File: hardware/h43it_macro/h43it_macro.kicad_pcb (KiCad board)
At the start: 2 copper layers, 90 x 90 mm, 43 parts, among them J1 Conn_01x04_Pin, SW2 SW_Push, U1 ATtiny816-M

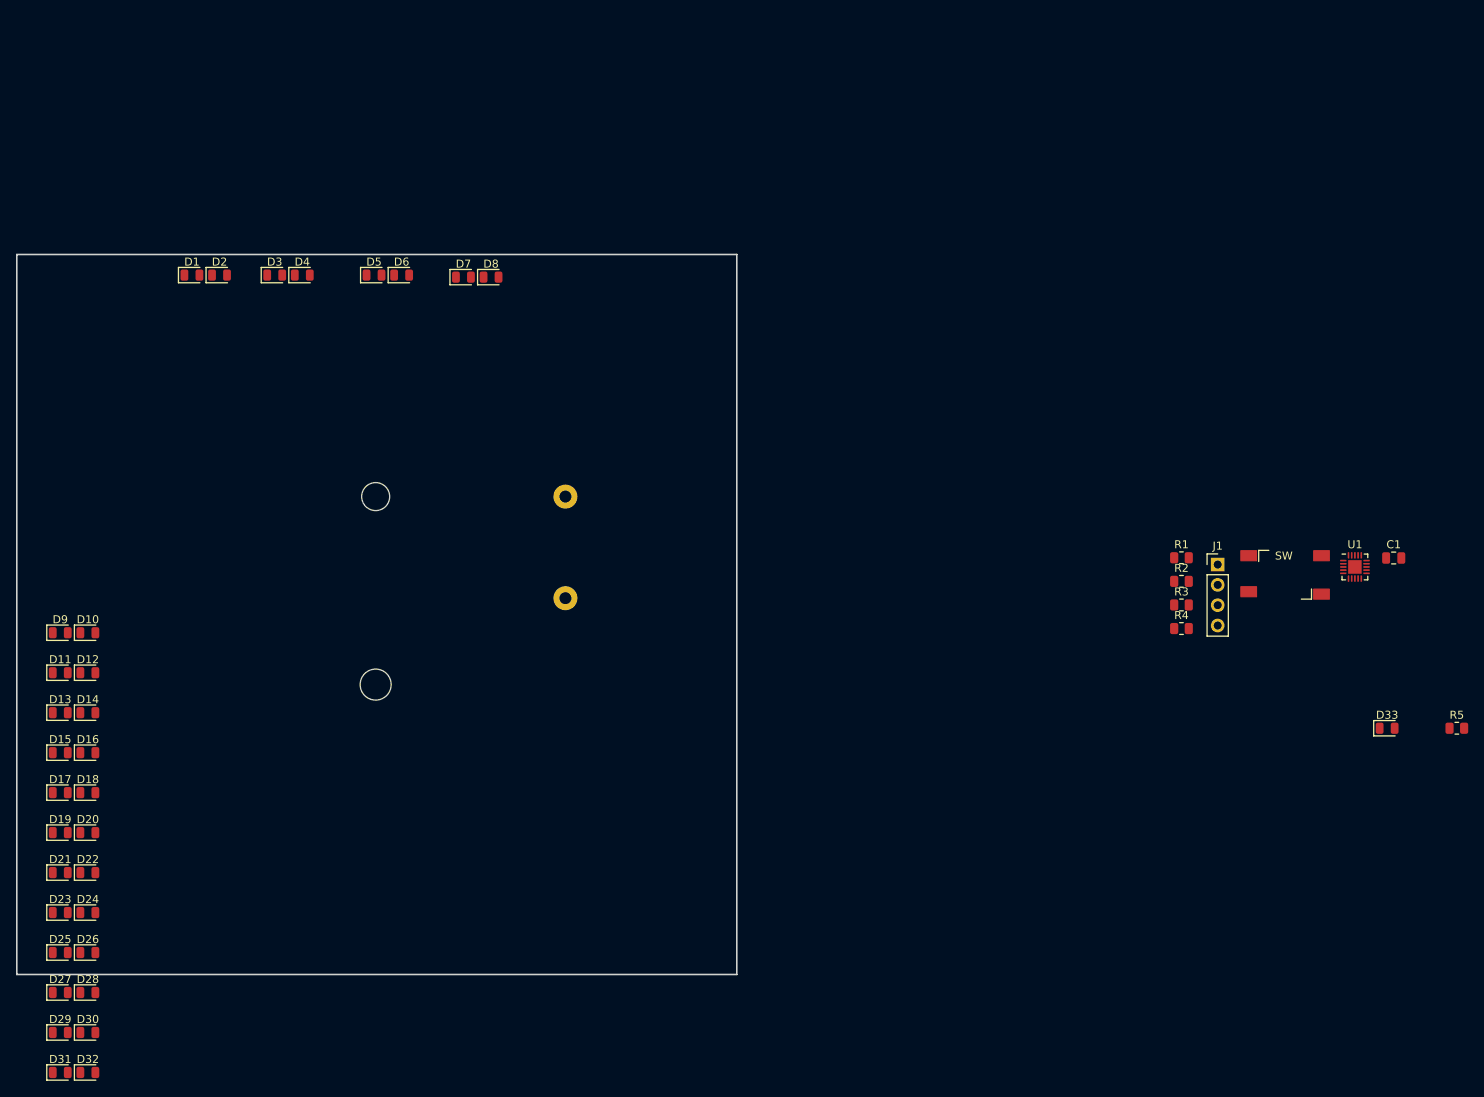
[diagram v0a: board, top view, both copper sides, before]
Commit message: add twin attiny 816
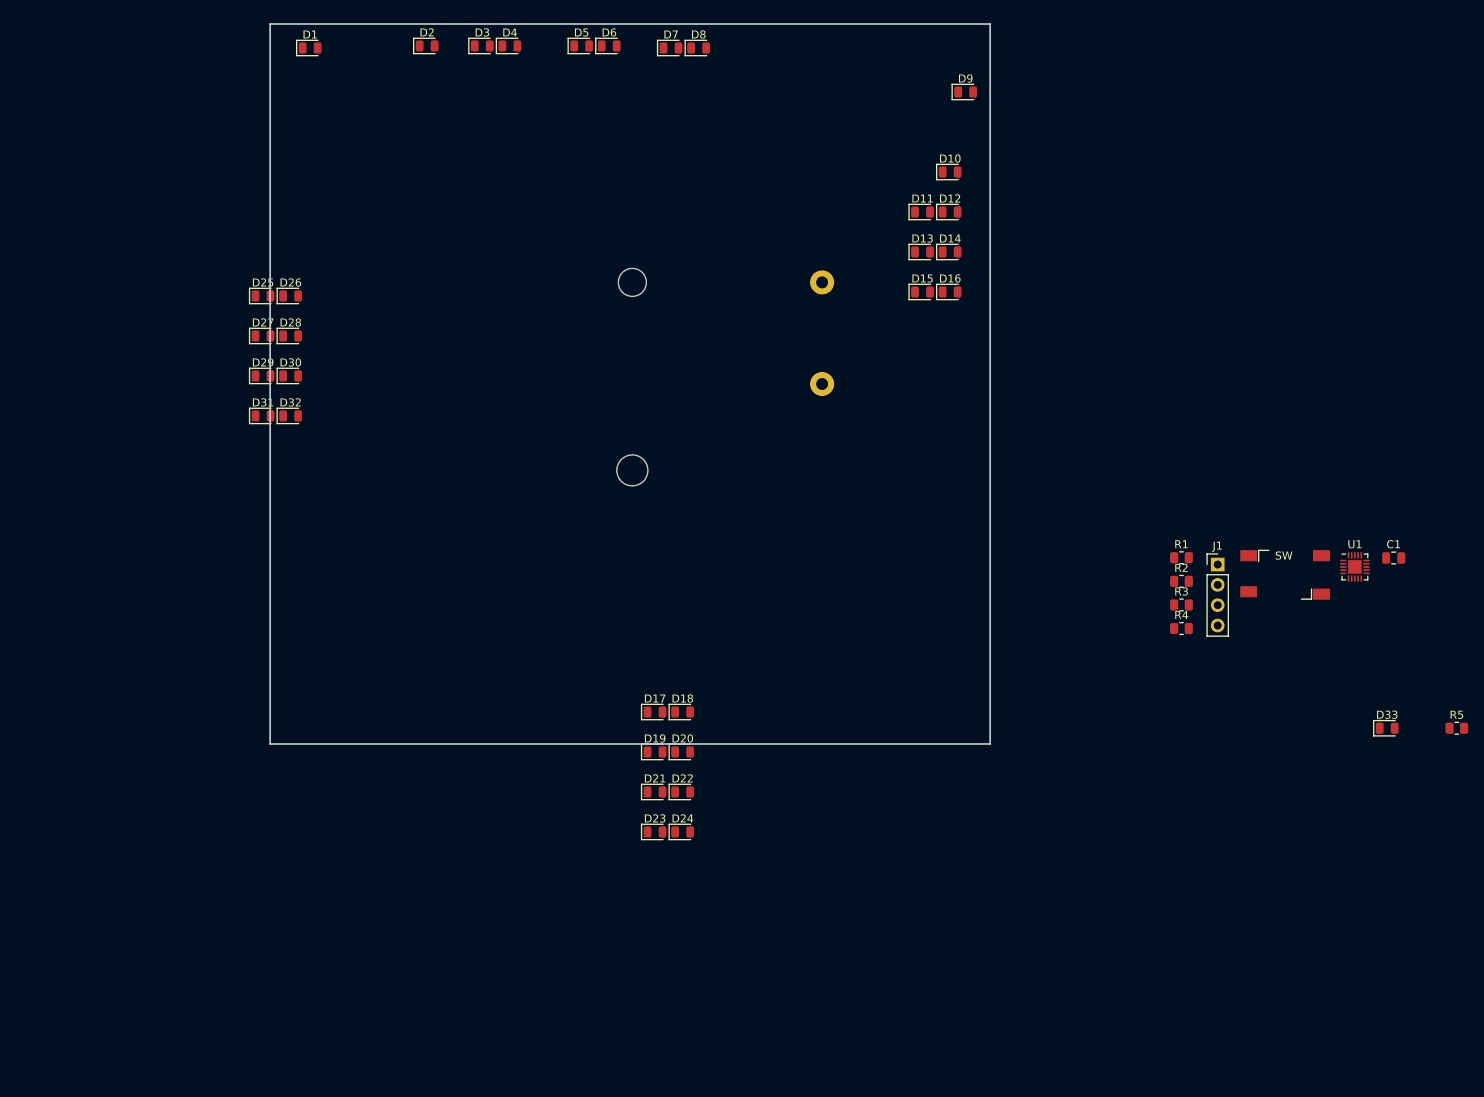
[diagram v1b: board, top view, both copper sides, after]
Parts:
- moved D9 131.8 mm to (156.9, 33.5)
- moved D10 122.2 mm to (155.0, 43.5)
- moved D11 122.2 mm to (151.6, 48.5)
- moved D12 122.2 mm to (155.0, 48.5)
- moved D13 122.2 mm to (151.6, 53.5)
- moved D14 122.2 mm to (155.0, 53.5)
- moved D15 122.2 mm to (151.6, 58.5)
- moved D16 122.2 mm to (155.0, 58.5)
- moved D25 85.9 mm to (69.1, 59.0)
- moved D26 85.9 mm to (72.6, 59.0)
- moved D29 85.9 mm to (69.1, 69.0)
- moved D30 85.9 mm to (72.6, 69.0)
- moved D27 85.9 mm to (69.1, 64.0)
- moved D28 85.9 mm to (72.6, 64.0)
- moved D31 85.9 mm to (69.1, 74.0)
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
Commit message: pcb for macro
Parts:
- removed U1: ATtiny816-M, Package_DFN_QFN:VQFN-20-1EP_3x3mm_P0.4mm_EP1.7x1.7mm
- added C2: 100pF, Capacitor_SMD:C_0805_2012Metric, F.Cu at (130.9, 100.0)
- added C3: 1uF, Capacitor_SMD:C_0805_2012Metric, F.Cu at (128.0, 100.0)
- added C4: 100pF, Capacitor_SMD:C_0805_2012Metric, F.Cu at (129.9, 95.0)
- added U2: ~, MyLib:TSOT32-6, F.Cu at (129.8, 89.6)
- added U4: ATtiny816-S, Package_SO:SOIC-20W_7.5x12.8mm_P1.27mm, F.Cu at (115.0, 94.1)
- added U6: ~, MyLib:TouchButton-15x10mm, F.Cu at (115.0, 70.0)
- BT1: footprint MyLib:Battery_holder_AAA_534-2479 -> MyLib:Battery_holder__Keystone_Electronic_AA_2462
- R5: value 100Ω -> 27Ω
- moved R5 119.0 mm to (100.9, 94.0), turned to 90 degrees
- moved D33 115.2 mm to (96.0, 94.0), turned to -90 degrees
- moved R4 105.2 mm to (84.4, 66.7)
- moved SW2 90.2 mm to (114.7, 56.3)
- moved R1 86.0 mm to (116.0, 38.9), turned to -90 degrees
- moved C1 84.6 mm to (126.0, 96.0)
- moved R3 68.7 mm to (116.0, 108.1), turned to 90 degrees
- moved J1 46.3 mm to (142.2, 90.3)
- moved D25 45.4 mm to (74.9, 104.0), turned to 180 degrees
- moved R2 45.0 mm to (148.6, 66.7)
- moved D17 30.2 mm to (148.4, 110.9), turned to -90 degrees
- moved BT1 25.0 mm to (115.0, 70.0)
- moved D8 23.9 mm to (147.4, 29.1)
- moved D10 23.8 mm to (154.4, 67.3)
- moved D11 23.8 mm to (150.9, 72.3)
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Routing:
- net Net-(U2-CX): track 0.00 -> 27.4 mm
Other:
- outline, holes or cut-outs redrawn
- board text added: "TOUCH ME!"

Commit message: pcb for macro
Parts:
- moved SW2 7.91 mm to (114.7, 48.4)
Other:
- board text added: "TOUCH ME IF YOU CAN"
- board text removed: "TOUCH ME!"
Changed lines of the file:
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@@
   )
   (footprint "MyLib:FSM2JSMAATR" (layer "F.Cu")
-    (at 114.746 56.32)
+    (at 114.746 48.41)
     (property "Sheetfile" "h43it_macro.kicad_sch")
     (property "Sheetname" "")
@@
   (gr_line locked (start 80 115) (end 150 115)
     (stroke (width 0.1) (type default)) (layer "Edge.Cuts"))
-  (gr_text "TOUCH ME!" (at 104.078 64.158) (layer "F.SilkS")
-    (effects (font (size 3 3) (thickness 0.3) bold) (justify left bottom))
+  (gr_text "TOUCH ME \nIF YOU CAN" (at 116.016 63.396) (layer "F.SilkS")
+    (effects (font (size 3 3) (thickness 0.3) bold) (justify bottom))
   )
   (segment (start 133 87) (end 131.326 88.674) (width 0.25) (layer "F.Cu") (net 28))

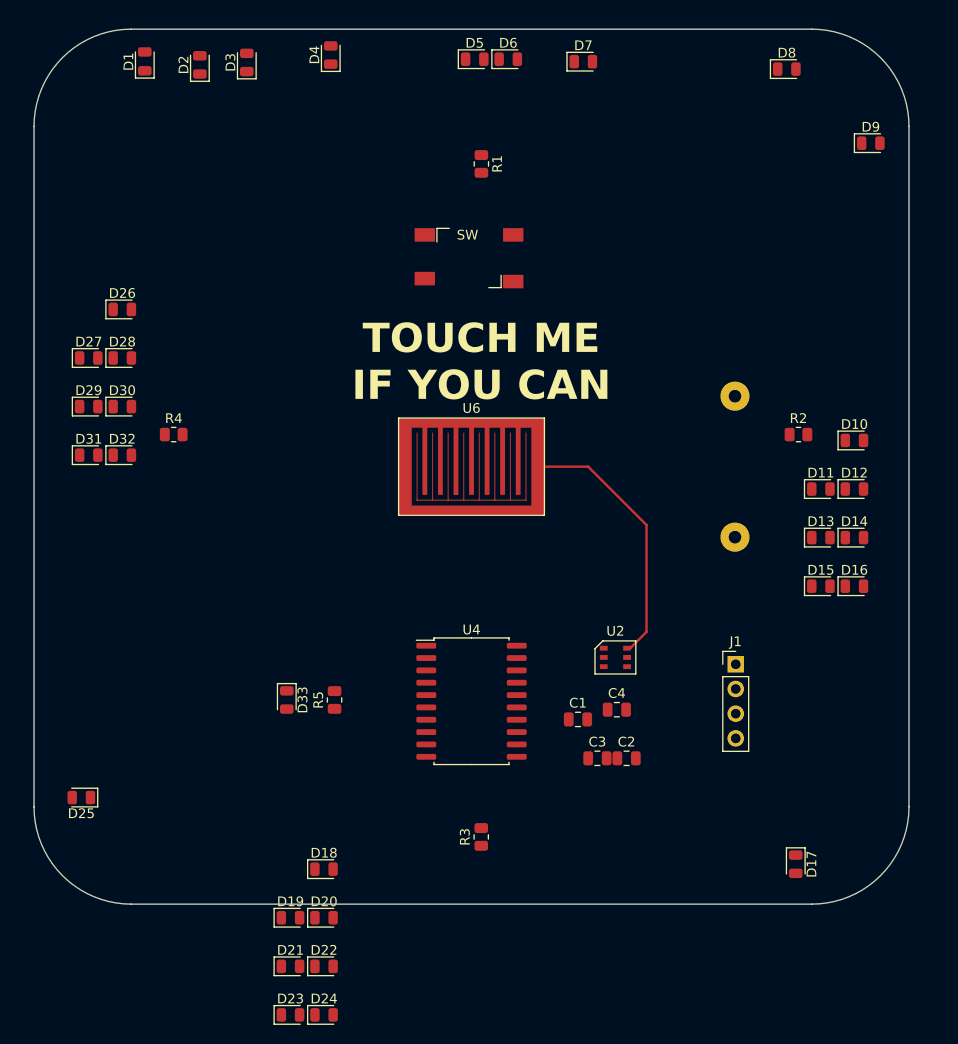
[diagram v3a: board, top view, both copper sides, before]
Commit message: pcb for macro 2
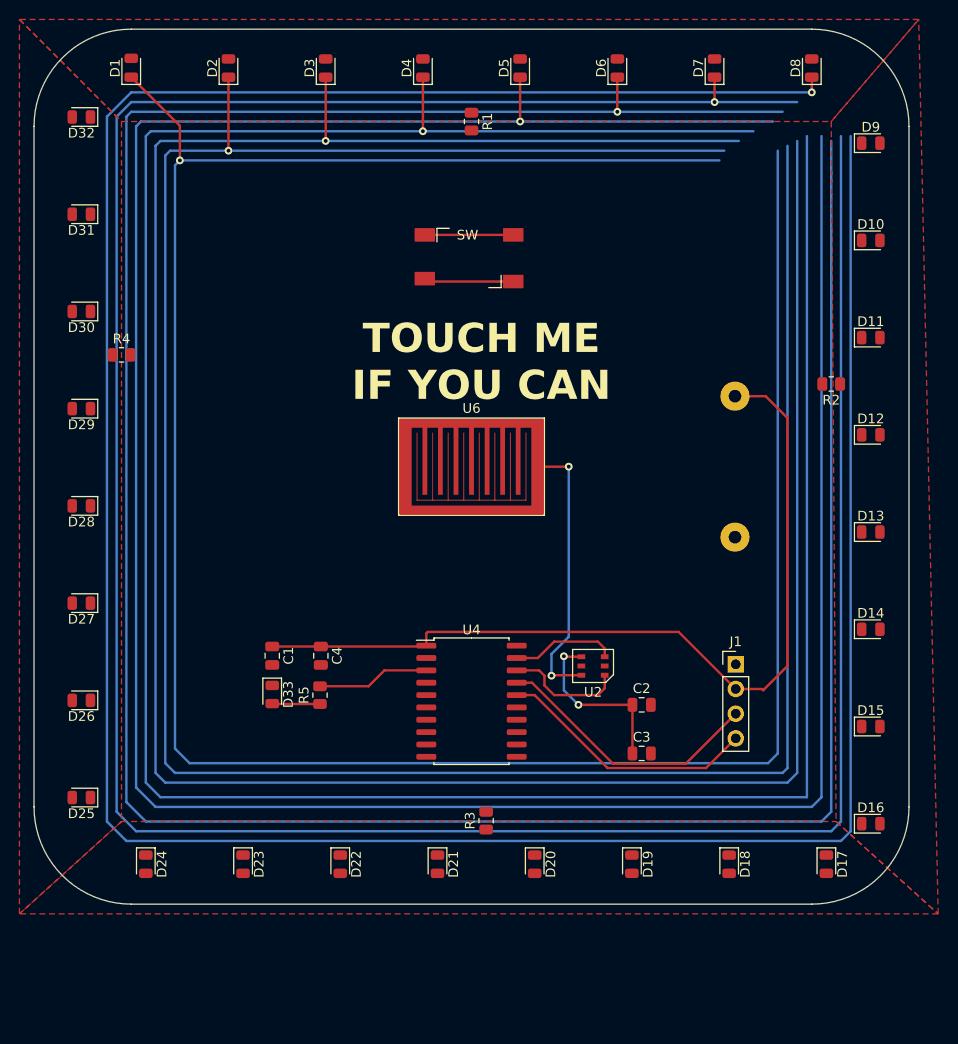
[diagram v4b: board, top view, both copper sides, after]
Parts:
- moved D18 41.7 mm to (141.5, 110.9), turned to -90 degrees
- moved D26 40.4 mm to (74.9, 94.0), turned to 180 degrees
- moved D19 35.5 mm to (131.5, 110.9), turned to -90 degrees
- moved D32 35.0 mm to (74.9, 34.0), turned to 180 degrees
- moved C1 32.1 mm to (94.5, 89.5), turned to -90 degrees
- moved C4 31.0 mm to (99.5, 89.5), turned to -90 degrees
- moved D27 25.2 mm to (74.9, 84.0), turned to 180 degrees
- moved D31 24.8 mm to (74.9, 44.0), turned to 180 degrees
- moved D16 24.5 mm to (156.1, 106.7)
- moved D24 24.0 mm to (81.5, 110.9), turned to -90 degrees
- moved D20 22.4 mm to (121.5, 110.9), turned to -90 degrees
- moved D10 20.6 mm to (156.1, 46.7)
- moved D21 18.4 mm to (111.5, 110.9), turned to -90 degrees
- moved D11 16.4 mm to (156.1, 56.7)
- moved D23 16.2 mm to (91.5, 110.9), turned to -90 degrees
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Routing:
- net /T-: track 0.00 -> 296.8 mm, vias 0 -> 1
- net /S-: track 0.00 -> 290.9 mm, vias 0 -> 1
- net /R-: track 0.00 -> 284.5 mm, vias 0 -> 1
- net /Q-: track 0.00 -> 278.0 mm, vias 0 -> 1
- net /P-: track 0.00 -> 271.4 mm, vias 0 -> 1
- net /O-: track 0.00 -> 263.1 mm, vias 0 -> 1
- net /N-: track 0.00 -> 256.4 mm, vias 0 -> 1
- net /M-: track 0.00 -> 251.9 mm, vias 0 -> 1
- net VCC: track 0.00 -> 89.7 mm
- net /TX: track 0.00 -> 28.1 mm
- net /UPDI: track 0.00 -> 26.9 mm
- net Net-(U2-VREG): track 0.00 -> 18.0 mm, vias 0 -> 2
- net /CapSens-IO1: track 0.00 -> 12.3 mm
- net /LED_ind: track 0.00 -> 11.6 mm
- net /CapSens-IO2: track 0.00 -> 10.9 mm
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- added copper zone on F.Cu, net Net-(D1-A)
- added copper zone on F.Cu, net Net-(D10-A)
- added copper zone on F.Cu, net Net-(D17-A)
- added copper zone on F.Cu, net Net-(D25-A)

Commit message: pcb for macro 3
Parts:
- moved SW2 34.6 mm to (115.0, 83.0)
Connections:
- U4 pad 18: /CapSens-IO1 -> /SW
- U4 pad 2: /SW -> /CapSens-IO1
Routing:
- net /A+: track 0.00 -> 112.6 mm, vias 0 -> 2
- net /D+: track 0.00 -> 71.1 mm, vias 0 -> 2
- net /B+: track 0.00 -> 61.0 mm, vias 0 -> 2
- net /T-: track 296.8 -> 356.5 mm, vias 1 -> 6
- net /Q-: track 278.0 -> 331.1 mm, vias 1 -> 4
- net /S-: track 290.9 -> 342.2 mm, vias 1 -> 4
- net /R-: track 284.5 -> 333.6 mm, vias 1 -> 4
- net /P-: track 271.4 -> 320.0 mm, vias 1 -> 3
- net /O-: track 263.1 -> 309.6 mm, vias 1 -> 4
- net /N-: track 256.4 -> 295.2 mm, vias 1 -> 4
- net /M-: track 251.9 -> 288.7 mm, vias 1 -> 4
- net /CapSens-IO1: track 12.3 -> 29.8 mm, vias 0 -> 2
- net /C+: track 0.00 -> 13.7 mm, vias 0 -> 2
- net GND: track 9.10 -> 20.1 mm, vias 0 -> 2
- net /SW: track 9.22 -> 19.4 mm, vias 0 -> 2
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- added copper zone on F.Cu, net GND
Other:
- outline, holes or cut-outs redrawn
- board text added: "H43it Macro V1 March 2024 Contact: j.jonas.peper@gmail.com"
